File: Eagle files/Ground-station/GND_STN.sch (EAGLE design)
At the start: 19 parts, among them U2 SOIC127P790X216-8NW25Q128JVJSQ

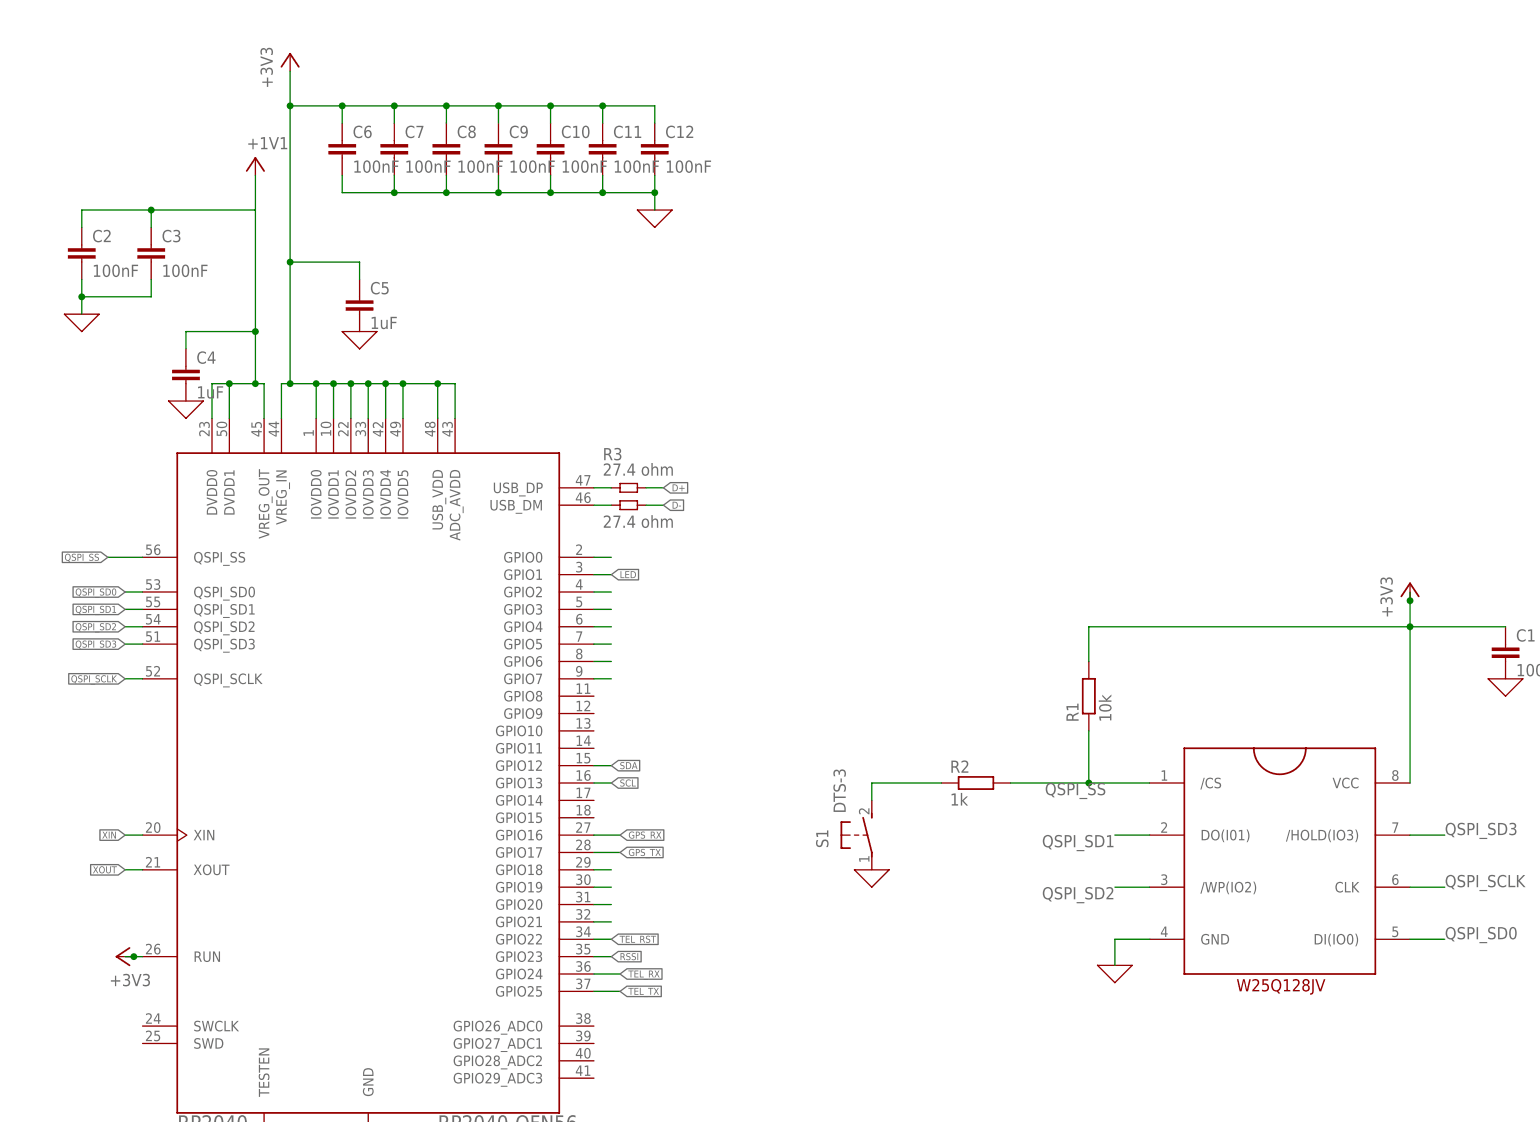
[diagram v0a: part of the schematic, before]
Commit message: Added the crystel oscillator to the board
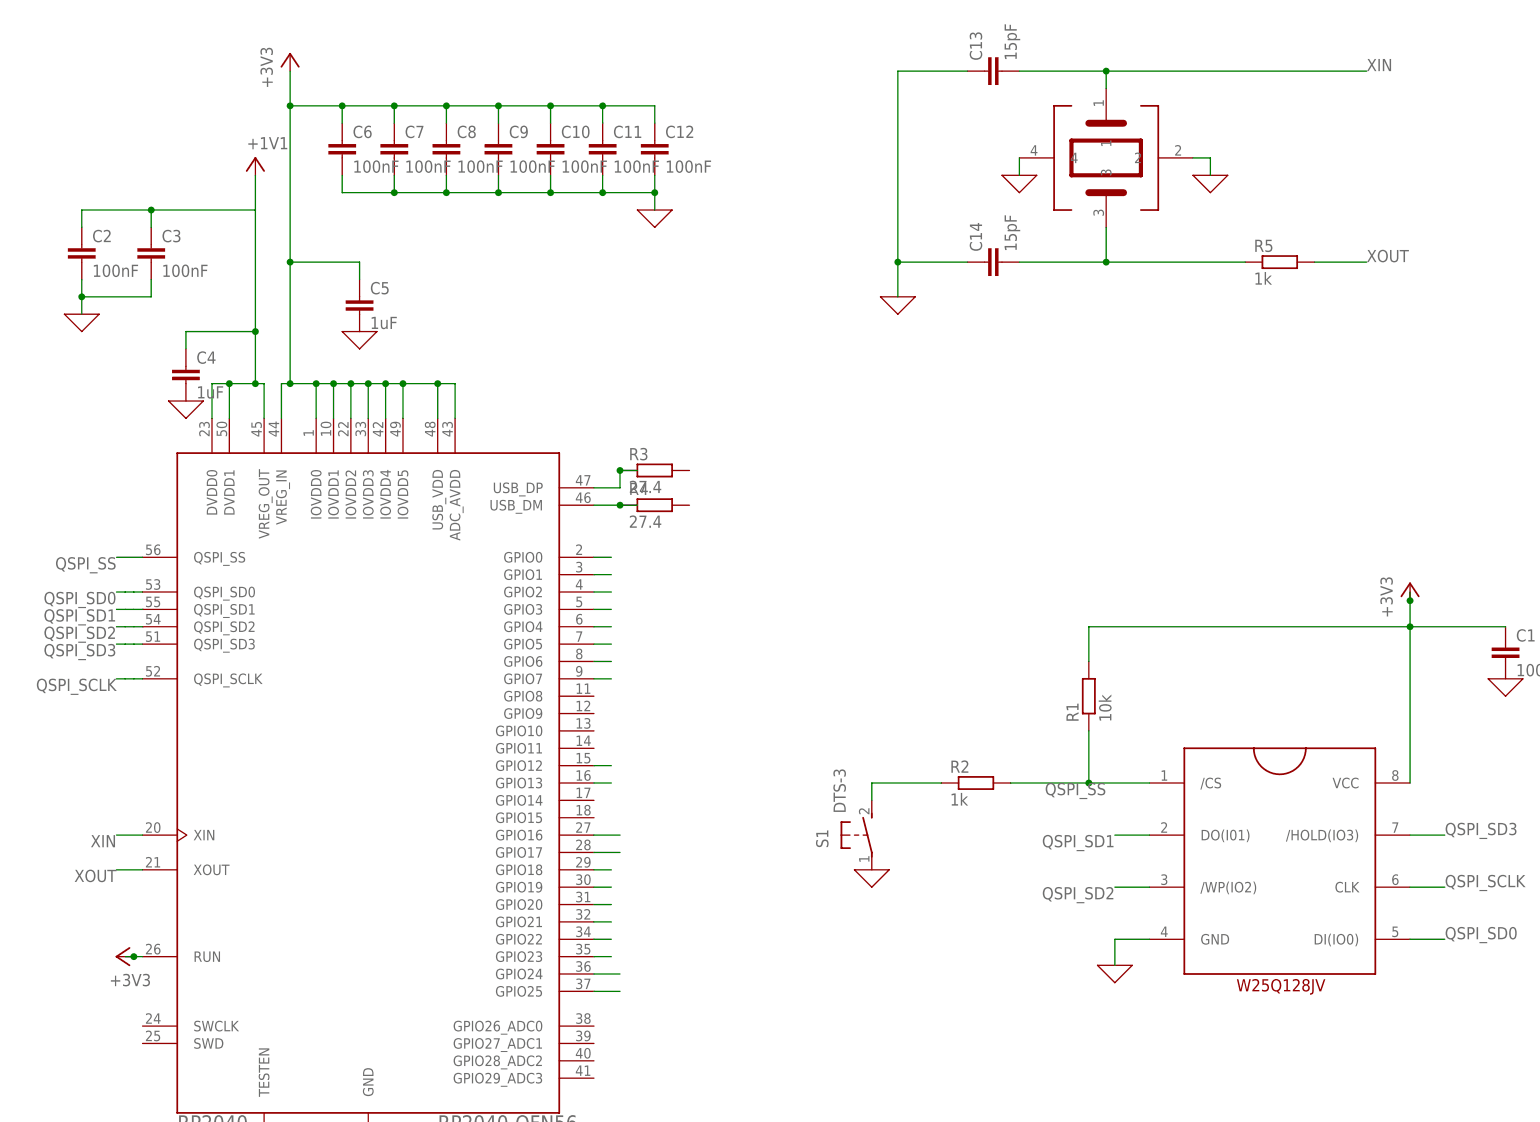
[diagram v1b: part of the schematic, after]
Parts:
- added C13, C14: 15pF, rcl:C-EUC0603
- added R5: 1k, rcl:R-EU_R0603
- added U$1: ABM8-272-T3, ABM8-272-T3:ABM8-272-T3
- R3, R4: value 27.4 ohm -> 27.4; device standardparts:RESISTOR.0603 -> rcl:R-EU_R0603
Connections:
- net USB_DM renamed N$4
- net USB_DP renamed N$3
- removed net D+: R3.2
- removed net D-: R4.2
- new net N$1: C14.2, R5.1, U$1.3
- net 0: now also C13.1, C14.1, U$1.2, U$1.4
- net XIN: now also C13.2, U$1.1
- net XOUT: now also R5.2

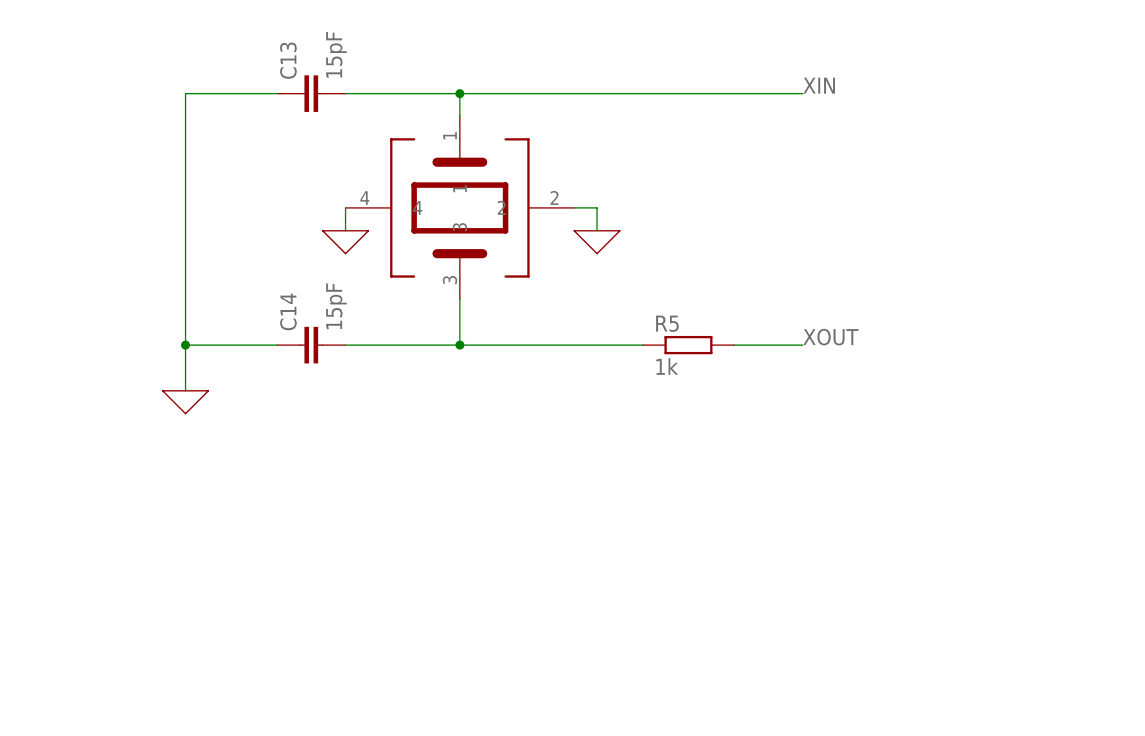
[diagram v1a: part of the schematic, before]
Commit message: Added USB-C and RESET button and corrections in Crystal Oscillator
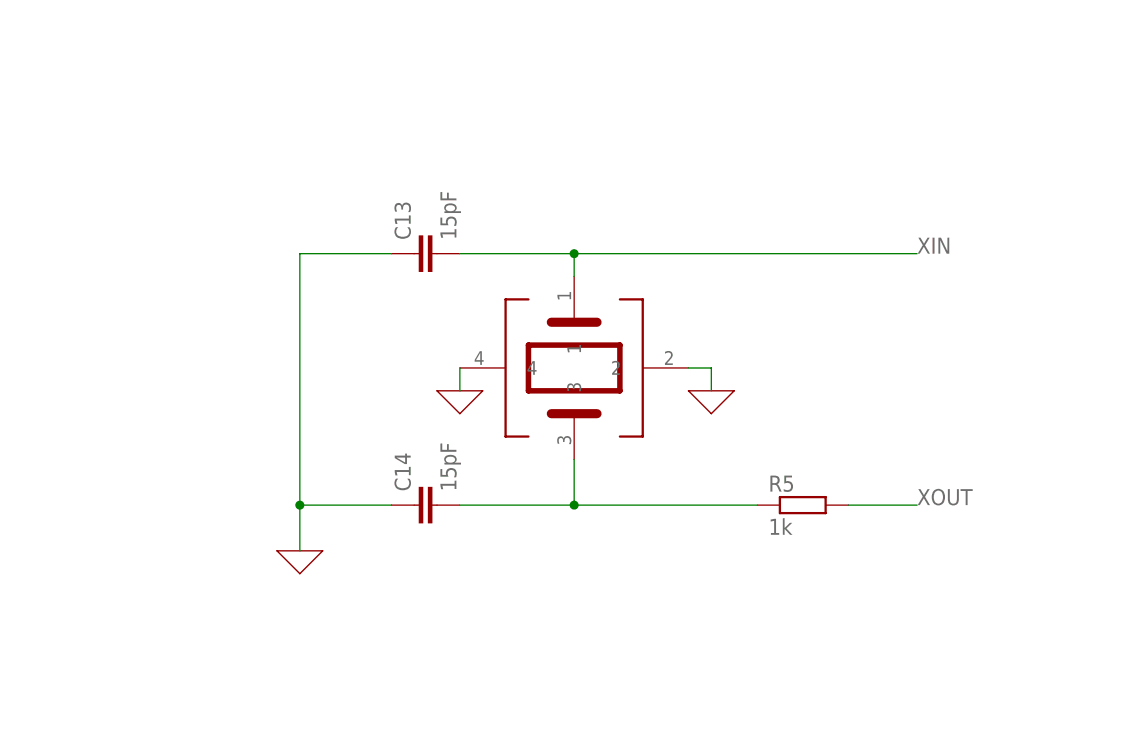
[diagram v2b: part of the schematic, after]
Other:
- moved on the sheet: C13, C14, R5
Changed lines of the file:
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@@
 <attribute name="VALUE" x="7.62" y="27.94" size="1.778" layer="96" rot="R180"/>
 </instance>
-<instance part="U$1" gate="G$1" x="147.32" y="147.32" smashed="yes"/>
-<instance part="R5" gate="G$1" x="172.72" y="132.08" smashed="yes">
-<attribute name="NAME" x="168.91" y="133.5786" size="1.778" layer="95"/>
-<attribute name="VALUE" x="168.91" y="128.778" size="1.778" layer="96"/>
+<instance part="U$1" gate="G$1" x="160.02" y="129.54" smashed="yes"/>
+<instance part="R5" gate="G$1" x="185.42" y="114.3" smashed="yes">
+<attribute name="NAME" x="181.61" y="115.7986" size="1.778" layer="95"/>
+<attribute name="VALUE" x="181.61" y="110.998" size="1.778" layer="96"/>
 </instance>
-<instance part="C13" gate="G$1" x="129.54" y="160.02" smashed="yes" rot="R90">
-<attribute name="NAME" x="129.159" y="161.544" size="1.778" layer="95" rot="R90"/>
-<attribute name="VALUE" x="134.239" y="161.544" size="1.778" layer="96" rot="R90"/>
+<instance part="C13" gate="G$1" x="142.24" y="142.24" smashed="yes" rot="R90">
+<attribute name="NAME" x="141.859" y="143.764" size="1.778" layer="95" rot="R90"/>
+<attribute name="VALUE" x="146.939" y="143.764" size="1.778" layer="96" rot="R90"/>
 </instance>
-<instance part="C14" gate="G$1" x="129.54" y="132.08" smashed="yes" rot="R90">
-<attribute name="NAME" x="129.159" y="133.604" size="1.778" layer="95" rot="R90"/>
-<attribute name="VALUE" x="134.239" y="133.604" size="1.778" layer="96" rot="R90"/>
+<instance part="C14" gate="G$1" x="142.24" y="114.3" smashed="yes" rot="R90">
+<attribute name="NAME" x="141.859" y="115.824" size="1.778" layer="95" rot="R90"/>
+<attribute name="VALUE" x="146.939" y="115.824" size="1.778" layer="96" rot="R90"/>
 </instance>
-<instance part="X_9" gate="G$1" x="116.84" y="127" smashed="yes"/>
-<instance part="X_10" gate="G$1" x="134.62" y="144.78" smashed="yes"/>
-<instance part="X_11" gate="G$1" x="162.56" y="144.78" smashed="yes"/>
+<instance part="X_9" gate="G$1" x="129.54" y="109.22" smashed="yes"/>
+<instance part="X_10" gate="G$1" x="147.32" y="127" smashed="yes"/>
+<instance part="X_11" gate="G$1" x="175.26" y="127" smashed="yes"/>
 <instance part="R3" gate="G$1" x="81.28" y="101.6" smashed="yes">
 <attribute name="NAME" x="77.47" y="103.0986" size="1.778" layer="95"/>
@@
 <segment>
 <pinref part="C13" gate="G$1" pin="1"/>
-<wire x1="127" y1="160.02" x2="116.84" y2="160.02" width="0.1524" layer="91"/>
+<wire x1="139.7" y1="142.24" x2="129.54" y2="142.24" width="0.1524" layer="91"/>
 <pinref part="C14" gate="G$1" pin="1"/>
-<wire x1="116.84" y1="160.02" x2="116.84" y2="132.08" width="0.1524" layer="91"/>
-<wire x1="116.84" y1="132.08" x2="127" y2="132.08" width="0.1524" layer="91"/>
-<wire x1="116.84" y1="132.08" x2="116.84" y2="127" width="0.1524" layer="91"/>
-<junction x="116.84" y="132.08"/>
+<wire x1="129.54" y1="142.24" x2="129.54" y2="114.3" width="0.1524" layer="91"/>
+<wire x1="129.54" y1="114.3" x2="139.7" y2="114.3" width="0.1524" layer="91"/>
+<wire x1="129.54" y1="114.3" x2="129.54" y2="109.22" width="0.1524" layer="91"/>
+<junction x="129.54" y="114.3"/>
 <pinref part="X_9" gate="G$1" pin="0"/>
 </segment>
 <segment>
 <pinref part="U$1" gate="G$1" pin="4"/>
-<wire x1="134.62" y1="147.32" x2="134.62" y2="144.78" width="0.1524" layer="91"/>
+<wire x1="147.32" y1="129.54" x2="147.32" y2="127" width="0.1524" layer="91"/>
 <pinref part="X_10" gate="G$1" pin="0"/>
 </segment>
 <segment>
 <pinref part="U$1" gate="G$1" pin="2"/>
-<wire x1="160.02" y1="147.32" x2="162.56" y2="147.32" width="0.1524" layer="91"/>
-<wire x1="162.56" y1="147.32" x2="162.56" y2="144.78" width="0.1524" layer="91"/>
+<wire x1="172.72" y1="129.54" x2="175.26" y2="129.54" width="0.1524" layer="91"/>
+<wire x1="175.26" y1="129.54" x2="175.26" y2="127" width="0.1524" layer="91"/>
 <pinref part="X_11" gate="G$1" pin="0"/>
 </segment>
@@
 <segment>
 <pinref part="U$1" gate="G$1" pin="1"/>
-<wire x1="147.32" y1="157.48" x2="147.32" y2="160.02" width="0.1524" layer="91"/>
-<wire x1="147.32" y1="160.02" x2="185.42" y2="160.02" width="0.1524" layer="91"/>
-<wire x1="147.32" y1="160.02" x2="134.62" y2="160.02" width="0.1524" layer="91"/>
-<junction x="147.32" y="160.02"/>
+<wire x1="160.02" y1="139.7" x2="160.02" y2="142.24" width="0.1524" layer="91"/>
+<wire x1="160.02" y1="142.24" x2="198.12" y2="142.24" width="0.1524" layer="91"/>
+<wire x1="160.02" y1="142.24" x2="147.32" y2="142.24" width="0.1524" layer="91"/>
+<junction x="160.02" y="142.24"/>
 <pinref part="C13" gate="G$1" pin="2"/>
-<label x="185.42" y="160.02" size="1.778" layer="95"/>
+<label x="198.12" y="142.24" size="1.778" layer="95"/>
 </segment>
 <segment>
@@
 <segment>
 <pinref part="R5" gate="G$1" pin="2"/>
-<wire x1="177.8" y1="132.08" x2="185.42" y2="132.08" width="0.1524" layer="91"/>
-<label x="185.42" y="132.08" size="1.778" layer="95"/>
+<wire x1="190.5" y1="114.3" x2="198.12" y2="114.3" width="0.1524" layer="91"/>
+<label x="198.12" y="114.3" size="1.778" layer="95"/>
 </segment>
 <segment>
@@
 <segment>
 <pinref part="U$1" gate="G$1" pin="3"/>
-<wire x1="147.32" y1="137.16" x2="147.32" y2="132.08" width="0.1524" layer="91"/>
-<wire x1="147.32" y1="132.08" x2="167.64" y2="132.08" width="0.1524" layer="91"/>
-<wire x1="147.32" y1="132.08" x2="134.62" y2="132.08" width="0.1524" layer="91"/>
-<junction x="147.32" y="132.08"/>
+<wire x1="160.02" y1="119.38" x2="160.02" y2="114.3" width="0.1524" layer="91"/>
+<wire x1="160.02" y1="114.3" x2="180.34" y2="114.3" width="0.1524" layer="91"/>
+<wire x1="160.02" y1="114.3" x2="147.32" y2="114.3" width="0.1524" layer="91"/>
+<junction x="160.02" y="114.3"/>
 <pinref part="R5" gate="G$1" pin="1"/>
 <pinref part="C14" gate="G$1" pin="2"/>

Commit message: .
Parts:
- removed C14: 15pF, rcl:C-EUC0603
- removed R3: 27.4, rcl:R-EU_R0603
- removed S1: DTS-3, DTS-3:DTS-3
- removed U$1: ABM8-272-T3, ABM8-272-T3:ABM8-272-T3
- added C15, C16: 100nF, rcl:C-EUC0603
- added C18: 10uF, rcl:C-EUC0805
- added C23, C24: 18pF, rcl:C-EUC0805
- added C40: 10 uF, standardparts:CAPACITOR.0603
- added D3, D4: SCHOTTKY_MBR0520LT1GDO-219, Diode:SCHOTTKY_MBR0520LT1GDO-219
- added IC1: BMP280, BMP280-standalone:BMP280
- added J2: XT60-M, XT60-M:XT60-M
- added Q3: SI7625DN-T1-GE3, SI7625DN-T1-GE3:SI7625DN-T1-GE3
- added R19, R23, R9: 10k, rcl:R-EU_R0805
- added R22: 1k, rcl:R-EU_R0805
- added R7: 5.1k ohm, standardparts:RESISTOR.0603
- added S3: DTS-3, DTS-3:DTS-3
- added SV1: (no value), con-lsta:FE10-1
- added U$2: HDC1080, Texas-HDC1080:HDC1080
- added U$3: ASE, crystal:ASE
- added U1: AMS1117-5.0, AMS1117-5.0:AMS1117-5.0
- added U4: SOIC127P790X216-8NW25Q128JVJSQ, SOIC127P790X216-8N:SOIC127P790X216-8NW25Q128JVJSQ
- added X1: USB Type C, microbuilder:USB_C
- added XBEE: XBP9B-XCST-021, XBP9B-XCST-021:XBP9B-XCST-021
- C1: value 100nF -> 10 uF; device rcl:C-EUC0603 -> standardparts:CAPACITOR.0603
- C13: value 15pF -> 22uF; device rcl:C-EUC0603 -> rcl:C-EUC0805
- C2: value 100nF -> 10uF; device rcl:C-EUC0603 -> rcl:C-EUC0805
- C3: value 100nF -> 22uF; device rcl:C-EUC0603 -> rcl:C-EUC0805
- C4, C5: value 1uF -> 100nF
- C6, C7: value 100nF -> 1uF
- R1: value 10k -> 1k; device rcl:R-EU_R0603 -> rcl:R-EU_R0805
- R2: value 1k -> 10k ohm; device rcl:R-EU_R0603 -> standardparts:RESISTOR.0603
- R4: value 27.4 -> 10k ohm; device rcl:R-EU_R0603 -> standardparts:RESISTOR.0603
- R5: value 1k -> 5.1k ohm; device rcl:R-EU_R0603 -> standardparts:RESISTOR.0603
- U2: value SOIC127P790X216-8NW25Q128JVJSQ -> AMS1117-3.3; device SOIC127P790X216-8N:SOIC127P790X216-8NW25Q128JVJSQ -> AMS1117-3.3:AMS1117-3.3
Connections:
- removed net +3V3: C1.1, C10.1, C11.1, C12.1, C5.1, C6.1, C7.1, C8.1, C9.1, R1.2, RP2040.ADC_AVDD, RP2040.IOVDD0, RP2040.IOVDD1, RP2040.IOVDD2, RP2040.IOVDD3, RP2040.IOVDD4, RP2040.IOVDD5, RP2040.RUN, RP2040.USB_VDD, RP2040.VREG_IN, U2.VCC
- removed net 0: C1.2, C10.2, C11.2, C12.2, C13.1, C14.1, C2.2, C3.2, C4.2, C5.2, C6.2, C7.2, C8.2, C9.2, RP2040.GND, RP2040.TESTEN, S1.1, U$1.2, U$1.4, U2.GND
- removed net BUZZER: RP2040.GPIO0
- removed net CAM: RP2040.GPIO2
- removed net CTRL: RP2040.GPIO3
- removed net DROGUE: RP2040.GPIO18
- removed net FIN_1: RP2040.GPIO7
- removed net FIN_2: RP2040.GPIO6
- removed net FIN_3: RP2040.GPIO5
- removed net FIN_4: RP2040.GPIO4
- removed net GPS_RX: RP2040.GPIO16
- removed net GPS_TX: RP2040.GPIO17
- removed net IGN1: RP2040.GPIO20
- removed net IGN2: RP2040.GPIO21
- removed net LED: RP2040.GPIO1
- removed net MAIN: RP2040.GPIO19
- removed net N$4: R4.1, RP2040.USB_DM
- removed net QSPI_SCLK: RP2040.QSPI_SCLK, U2.CLK
- removed net QSPI_SD0: RP2040.QSPI_SD0, U2.DI(IO0)
- removed net QSPI_SD1: RP2040.QSPI_SD1, U2.DO(I01)
- removed net QSPI_SD2: RP2040.QSPI_SD2, U2./WP(IO2)
- removed net QSPI_SD3: RP2040.QSPI_SD3, U2./HOLD(IO3)
- removed net QSPI_SS: R1.1, R2.2, RP2040.QSPI_SS, U2./CS
- new net 3V3: C1.2, C13.1, C40.2, IC1.VDD, IC1.VDDIO, R19.2, R23.2, R4.2, R9.1, SV1.2, SV1.9, U$2.VDD, U2.VOUT, XBEE.VCC
- new net 3V3_OP: C10.1, C11.1, C12.1, C15.1, C16.1, C7.1, C8.1, C9.1, RP2040.ADC_AVDD, RP2040.IOVDD0, RP2040.IOVDD1, RP2040.IOVDD2, RP2040.IOVDD3, RP2040.IOVDD4, RP2040.IOVDD5, RP2040.RUN, RP2040.USB_VDD, RP2040.VREG_IN, U4.VCC
- new net 5V: D3.C, Q3.D_1, Q3.D_2, Q3.D_3, Q3.D_4, Q3.D_5, Q3.D_6, Q3.D_7, U2.VIN
- new net 5V_BATT: C3.1, D4.C, Q3.S_1, Q3.S_2, Q3.S_3, U1.VOUT
- new net 5V_USB: D3.A, X1.VBUS
- new net CC3: R5.1, X1.CC2
- new net CC4: R7.1, X1.CC1
- new net CSB: IC1.CSB, R4.1
- new net CS_TFT: RP2040.GPIO5, SV1.7
- new net CTS: XBEE.NCTS/DIO7
- new net D+: X1.D+
- new net D-: X1.D-
- new net DC: RP2040.GPIO6, SV1.5
- new net DTR: XBEE.NDTR/SLEEP_RQ/DIO8
- new net FLASH_CLK: RP2040.QSPI_SCLK, U4.CLK
- new net FLASH_CS: R19.1, R22.2, RP2040.QSPI_SS, U4./CS
- new net FLASH_DI: RP2040.QSPI_SD0, U4.DI(IO0)
- new net FLASH_DO: RP2040.QSPI_SD1, U4.DO(I01)
- new net FLASH_HOLD: RP2040.QSPI_SD3, U4./HOLD(IO3)
- new net FLASH_WP: RP2040.QSPI_SD2, U4./WP(IO2)
- new net GND: C1.1, C10.2, C11.2, C12.2, C13.2, C15.2, C16.2, C18.2, C2.2, C23.2, C24.1, C3.2, C4.2, C40.1, C5.2, C6.2, C7.2, C8.2, C9.2, IC1.GND, J2.NEG, R2.1, R5.2, R7.2, RP2040.GND, RP2040.TESTEN, S3.1, SV1.8, U$2.GND, U$3.GND, U$3.VDD, U1.GND/ADJ, U2.GND/ADJ, U4.GND, X1.GND, XBEE.GND
- new net MISO: RP2040.GPIO4, SV1.1
- new net MOSI: RP2040.GPIO3, SV1.4
- new net N$16: C18.1, J2.POS, U1.VIN
- new net Q1-G: Q3.G
- new net RST_TFT: RP2040.GPIO7, SV1.6
- new net RTS: XBEE.NRTS/DIO6
- new net SCK: RP2040.GPIO10, RP2040.GPIO2, SV1.3
- new net SDO1: IC1.SDO, R2.2
- new net SUPP_TFT: RP2040.GPIO8, SV1.10
- net 1V1: now also C5.1, C6.1; no longer C2.1, C3.1
- net N$1: now also D4.A; no longer C14.2, R5.1, U$1.3
- net N$2: now also R22.1, S3.2; no longer R2.1, S1.2
- net N$3: now also C2.1; no longer R3.1, RP2040.USB_DP
- net RSSI: now also XBEE.DIO10/PWM0; no longer RP2040.GPIO23
- net SCL: now also IC1.SCK, R9.2, RP2040.GPIO11, U$2.SCL; no longer RP2040.GPIO13
- net SDA: now also IC1.SDI, R23.1, U$2.SDA
- net TEL_RST: now also XBEE.!RESET; no longer RP2040.GPIO22
- net TEL_RX: now also XBEE.DIN/NCONFIG/DIO14; no longer RP2040.GPIO24
- net TEL_TX: now also XBEE.DOUT/DIO13; no longer RP2040.GPIO25
- net XIN: now also C23.1, U$3.OUT; no longer C13.2, U$1.1
- net XOUT: now also C24.2, R1.1, R1.2, U$3.TRI; no longer R5.2
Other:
- note added: "BMP280"
- note added: "Crystal Oscillator"
- note added: "Flash chip (W25Q125JV)"
- note added: "Humidity Sensor"
- note added: "I2C0 bus is used I2C register is 0x76 as SD0 is pulled low"
- note added: "Power Supply"
- note added: "TFT LCD Display Header Pins"
- note added: "Use YSX321SL 12pF 10PPM oscillator. If of different load resistance change the C23 and C24."
- note added: "XBEE??"
- note removed: "GROUND STATION COMPUTER"
- moved on the sheet: C10, C11, C12, C13, C2, C4, C5, C6, C7, C8, C9, R1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
